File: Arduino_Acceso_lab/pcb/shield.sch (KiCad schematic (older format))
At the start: 34 parts, among them K1 RELAY_C, K2 RELAY_C, P1 Power, P10 Sensor1, P11 Sensor2, P12 Luz1, P13 Luz2, P2 Analog, P3 Digital, P4 Digital, P5 modulo esp8266, P6 fuente, P7 buzzer 1, P8 buzzer 2, P9 Timer RTC, Q1 2N2222, Q2 2N2222, U1 LM2576

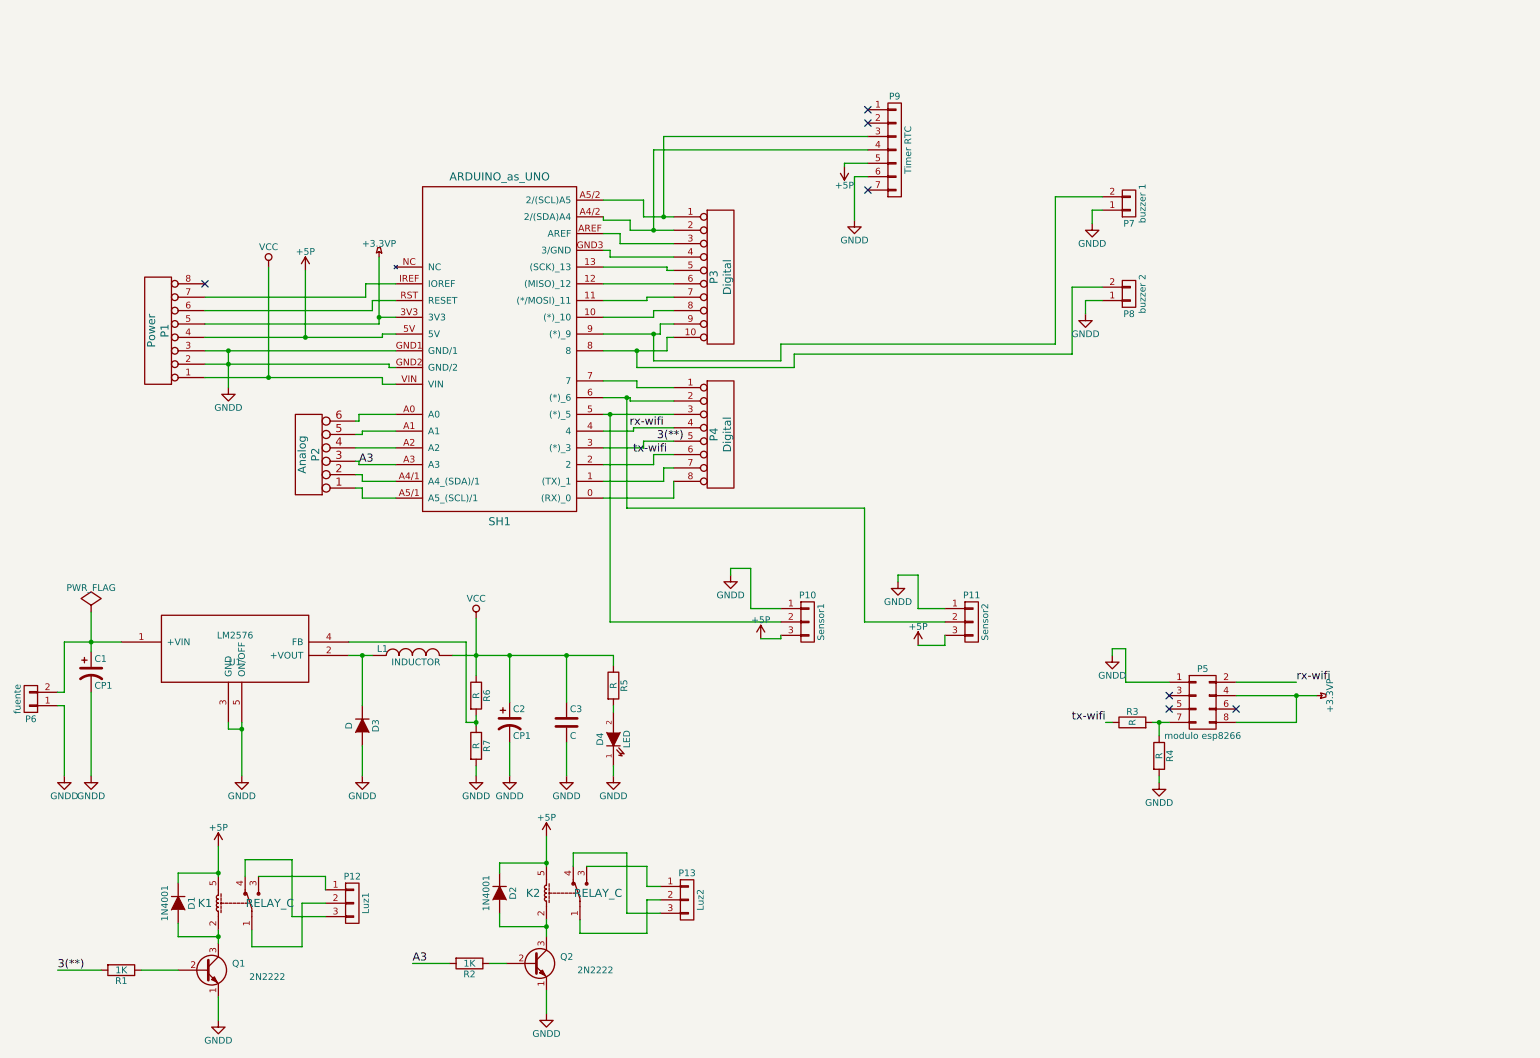
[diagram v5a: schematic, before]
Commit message: Detalles pcb acceso arduino lab.
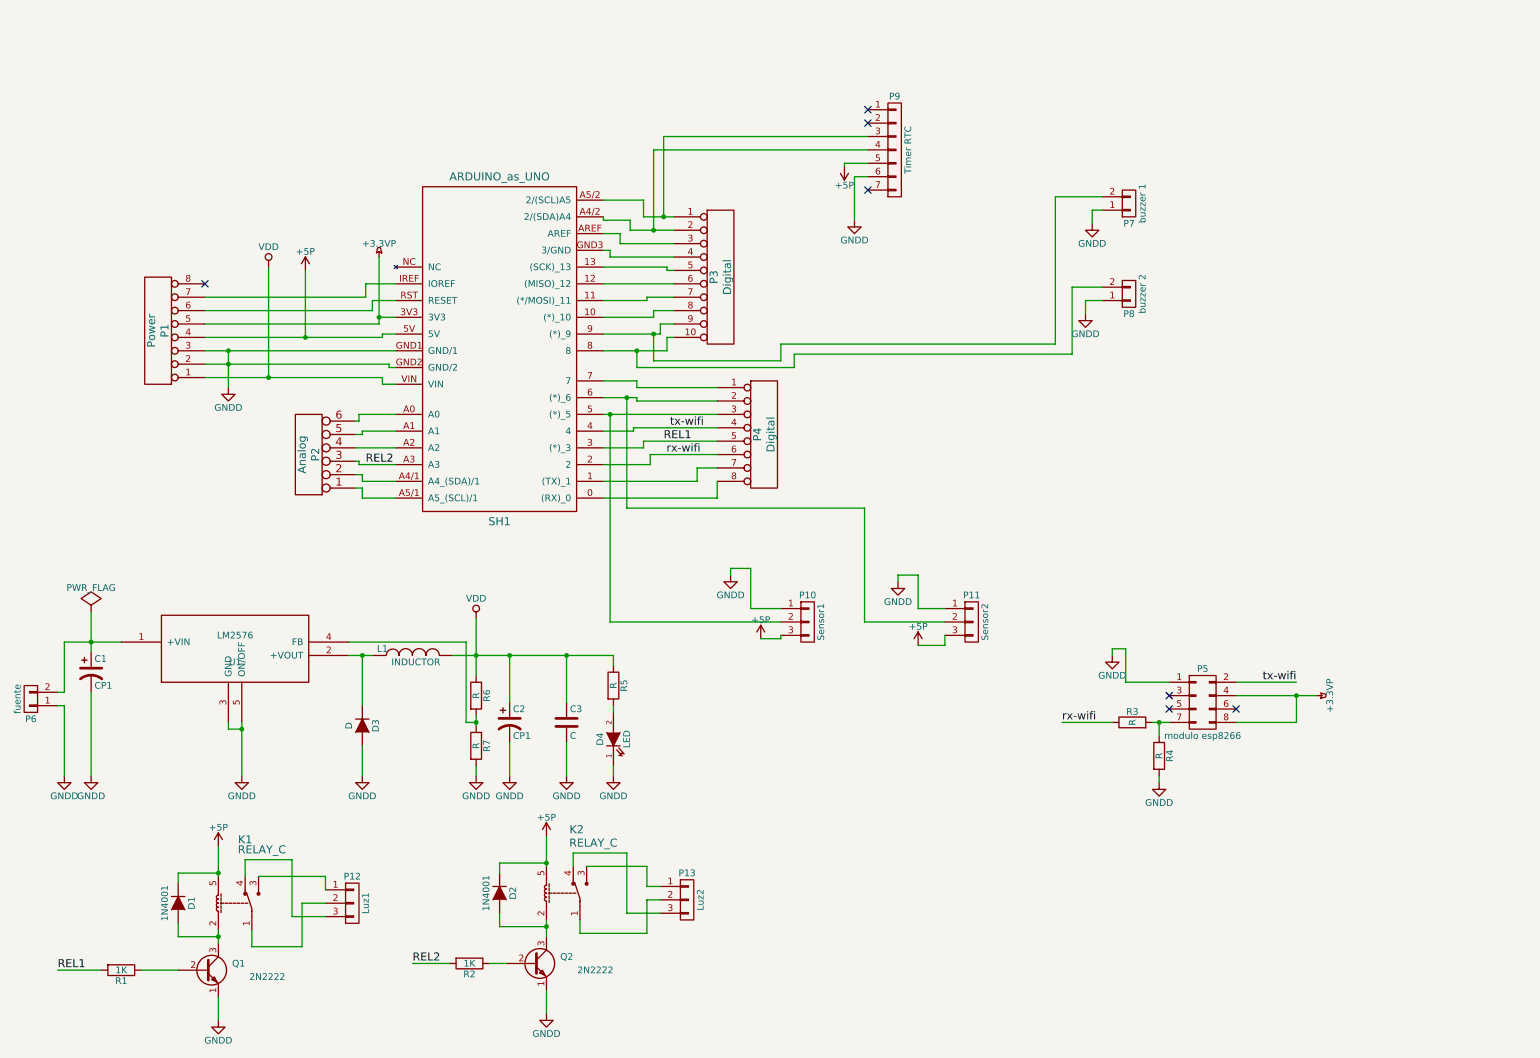
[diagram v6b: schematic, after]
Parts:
- P6: footprint Connect:PINHEAD1-2 -> Connect:bornier2
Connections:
- net rx-wifi: now also P4.6 (P6), R3.1, SH1.2; no longer P4.4 (P4), P5.2 (P2), SH1.4
- net tx-wifi: now also P4.4 (P4), P5.2 (P2), SH1.4; no longer P4.6 (P6), R3.1, SH1.2
- net VDD: now reaches P1.1 (P1), SH1.VIN
- net VDD: now also C2.1, C3.1, L1.2, R5.1, R6.1
- net 3(**) renamed REL1
- net A3 renamed REL2
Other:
- moved on the sheet: P4
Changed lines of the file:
@@
 EESchema Schematic File Version 2
 LIBS:shield-rescue
-LIBS:acceso
 LIBS:power
-LIBS:device
-LIBS:transistors
-LIBS:shield_arduino
-LIBS:conn
-LIBS:lm2576
 LIBS:shield-cache
 EELAYER 25 0
@@
 Sheet 1 1
 Title "shield sist. monitoreo"
-Date "lun. 30 mars 2015"
+Date "2016-11-14"
 Rev ""
-Comp "Costa Leonel"
+Comp "Costa Leonel y Alejandro Franco"
 Comment1 ""
 Comment2 ""
@@
 NoConn ~ 6875 1400
 Text Label 825  7225 0    60   ~ 0
-3(**)
+REL1
 Text Label 3475 7175 0    60   ~ 0
-A3
+REL2
 $Comp
 L CONN_01X03 P12
@@
 U 1 1 578FD508
 P 2175 6725
-F 0 "K1" V 2175 6975 60  0000 C CNN
-F 1 "RELAY_C" V 2175 6490 60  0000 C CNN
+F 0 "K1" V 2650 6675 60  0000 C CNN
+F 1 "RELAY_C" V 2575 6550 60  0000 C CNN
 F 2 "Poncho_PLC:Relay_C" H 2175 6725 60  0001 C CNN
 F 3 "" H 2175 6725 60  0000 C CNN
@@
 U 1 1 578FD787
 P 4625 6650
-F 0 "K2" V 4625 6900 60  0000 C CNN
-F 1 "RELAY_C" V 4625 6415 60  0000 C CNN
+F 0 "K2" V 5100 6575 60  0000 C CNN
+F 1 "RELAY_C" V 5000 6450 60  0000 C CNN
 F 2 "Poncho_PLC:Relay_C" H 4625 6650 60  0001 C CNN
 F 3 "" H 4625 6650 60  0000 C CNN
@@
 	1    0    0    -1
 $EndComp
-Text Label 3075 3450 0    60   ~ 0
-A3
-Text Label 5300 3275 0    60   ~ 0
-3(**)
+Text Label 3125 3450 0    60   ~ 0
+REL2
+Text Label 5350 3275 0    60   ~ 0
+REL1
 $Comp
 L ARDUINO_as_UNO-RESCUE-shield SH1
@@
 L CONN_8 P4
 U 1 1 5797E46E
-P 5775 3225
-F 0 "P4" V 5725 3225 60  0000 C CNN
-F 1 "Digital" V 5825 3225 60  0000 C CNN
-F 2 "Socket_Strips:Socket_Strip_Straight_1x08" H 5775 3225 60  0001 C CNN
-F 3 "" H 5775 3225 60  0000 C CNN
-	1    5775 3225
+P 6100 3225
+F 0 "P4" V 6050 3225 60  0000 C CNN
+F 1 "Digital" V 6150 3225 60  0000 C CNN
+F 2 "Socket_Strips:Socket_Strip_Straight_1x08" H 6100 3225 60  0001 C CNN
+F 3 "" H 6100 3225 60  0000 C CNN
+	1    6100 3225
 	1    0    0    -1
 $EndComp
@@
 9F 9A D9 D9 D9 5B B7 6E 5D B5 6A 15 F2 E4 79 3C 9E 19 33 66 24 24 04 E6 42 3A 7B F6 EC 5B 6F BD
 75 74 74 94 E3 8F 3E 9F 8F DB B9 80 A7 F5 69 62 62 22 A0 BE C1 70 3F C1 FF 07 F5 DC 9C 93 4E 27
-13 5B 00 00 00 00 49 45 4E 44 AE 42 60 82 9F
+13 5B 00 00 00 00 49 45 4E 44 AE 42 60 82 00
 EndData
 $EndBitmap
@@
 EndData
 $EndBitmap
-Text Label 10075 5075 0    60   ~ 0
+Text Label 8325 5375 0    60   ~ 0
 rx-wifi
 $Comp
@@
 F 0 "P6" H 625 5350 50  0000 C CNN
 F 1 "fuente" V 725 5200 50  0000 C CNN
-F 2 "Connect:PINHEAD1-2" H 625 5200 50  0001 C CNN
+F 2 "Connect:bornier2" H 625 5200 50  0001 C CNN
 F 3 "" H 625 5200 50  0000 C CNN
 	1    625  5200
@@
 	1    0    0    1
 $EndComp
-Text Label 5350 3175 2    60   ~ 0
+Text Label 5625 3375 2    60   ~ 0
 rx-wifi
-Text Label 5375 3375 2    60   ~ 0
+Text Label 5650 3175 2    60   ~ 0
 tx-wifi
-Text Label 8650 5375 2    60   ~ 0
+Text Label 10075 5075 2    60   ~ 0
 tx-wifi
 $Comp
@@
 	4900 2350 5275 2350
 Wire Wire Line
-	5150 2875 5425 2875
+	5150 2875 5750 2875
 Wire Wire Line
 	5150 2825 5150 2875
@@
 	4900 2825 5150 2825
 Wire Wire Line
-	5100 2950 5100 2975
+	5150 2950 5150 2975
 Wire Wire Line
 	5125 3200 5125 3175
@@
 	4900 3325 5200 3325
 Wire Wire Line
-	5275 3450 5275 3375
+	5250 3450 5250 3375
 Wire Wire Line
-	4900 3450 5275 3450
+	4900 3450 5250 3450
 Wire Wire Line
-	5350 3475 5425 3475
+	5600 3475 5750 3475
 Wire Wire Line
-	5350 3575 5350 3475
+	5600 3575 5600 3475
 Wire Wire Line
-	4900 3575 5350 3575
+	4900 3575 5600 3575
 Wire Wire Line
-	5425 3700 5425 3575
+	5750 3700 5750 3575
 Wire Wire Line
-	4900 3700 5425 3700
+	4900 3700 5750 3700
 Wire Wire Line
 	3100 3700 3350 3700
@@
 Connection ~ 9050 5375
 Wire Wire Line
-	8700 5375 8650 5375
+	8325 5375 8700 5375
 Wire Wire Line
 	5350 1000 5350 1600
@@
 	8275 1450 8275 2550
 Wire Wire Line
-	5125 3175 5425 3175
+	5125 3175 5750 3175
 Wire Wire Line
-	5200 3275 5425 3275
+	5200 3275 5750 3275
 Wire Wire Line
-	5275 3375 5425 3375
+	5250 3375 5750 3375
 Wire Wire Line
 	3050 3425 3075 3425
@@
 	3225 2400 1925 2400
 Wire Wire Line
-	3250 2500 1925 2500
+	1925 2500 3250 2500
 Wire Wire Line
-	5100 2975 5425 2975
+	5150 2975 5750 2975
 Wire Wire Line
 	6000 4225 5850 4225
@@
 	6850 4625 7450 4625
 Wire Wire Line
-	4900 3075 5425 3075
+	4900 3075 5750 3075
 Wire Wire Line
 	4950 3075 4950 4625
 Connection ~ 4950 3075
 Wire Wire Line
-	4900 2950 5100 2950
+	4900 2950 5150 2950
 Wire Wire Line
 	5075 2950 5075 3775
@@
 Wire Wire Line
 	875  5250 875  5775
-$Comp
-L VCC #PWR01
-U 1 1 581CF548
-P 3950 4600
-F 0 "#PWR01" H 3950 4450 50  0001 C CNN
-F 1 "VCC" H 3950 4750 50  0000 C CNN
-F 2 "" H 3950 4600 50  0000 C CNN
-F 3 "" H 3950 4600 50  0000 C CNN
-	1    3950 4600
-	1    0    0    -1
-$EndComp
-$Comp
-L VCC #PWR02
-U 1 1 581CFCCF
-P 2400 1975
-F 0 "#PWR02" H 2400 1825 50  0001 C CNN
-F 1 "VCC" H 2400 2125 50  0000 C CNN
-F 2 "" H 2400 1975 50  0000 C CNN
-F 3 "" H 2400 1975 50  0000 C CNN
-	1    2400 1975
-	1    0    0    -1
-$EndComp
 Connection ~ 3225 2350
 Wire Wire Line
@@
 	2675 2000 2675 2500
 Connection ~ 2675 2500
+$Comp
+L VDD #PWR?
+U 1 1 582A51D7
+P 2400 1975
+F 0 "#PWR?" H 2400 1825 50  0001 C CNN
+F 1 "VDD" H 2400 2125 50  0000 C CNN
+F 2 "" H 2400 1975 50  0000 C CNN
+F 3 "" H 2400 1975 50  0000 C CNN
+	1    2400 1975
+	1    0    0    -1
+$EndComp
+$Comp
+L VDD #PWR?
+U 1 1 582A5442
+P 3950 4600
+F 0 "#PWR?" H 3950 4450 50  0001 C CNN
+F 1 "VDD" H 3950 4750 50  0000 C CNN
+F 2 "" H 3950 4600 50  0000 C CNN
+F 3 "" H 3950 4600 50  0000 C CNN
+	1    3950 4600
+	1    0    0    -1
+$EndComp
 $EndSCHEMATC
